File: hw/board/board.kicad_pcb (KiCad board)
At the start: 4 copper layers, 100 x 85 mm, 52 parts, among them U1 XC7A35T-FTG256, U2 TPS54331DR

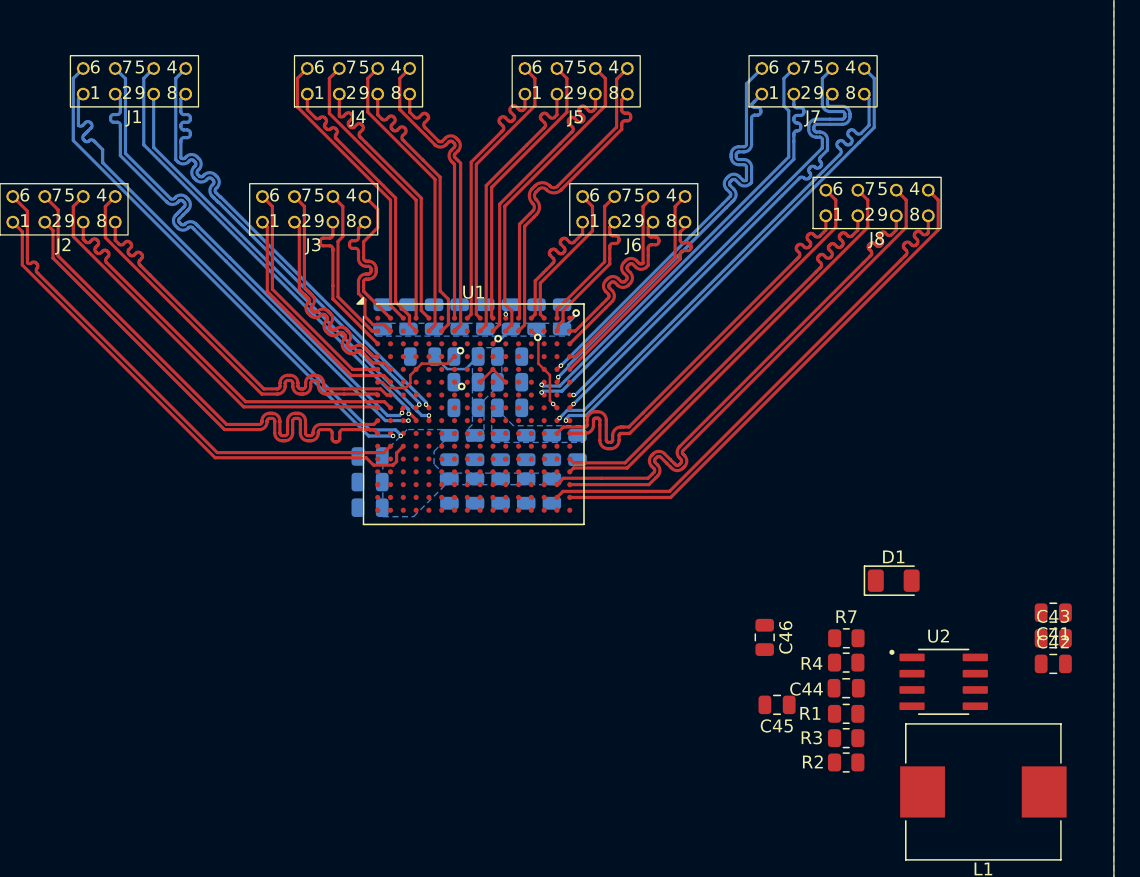
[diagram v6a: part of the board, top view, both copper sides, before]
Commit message: Routed all voltage regulators
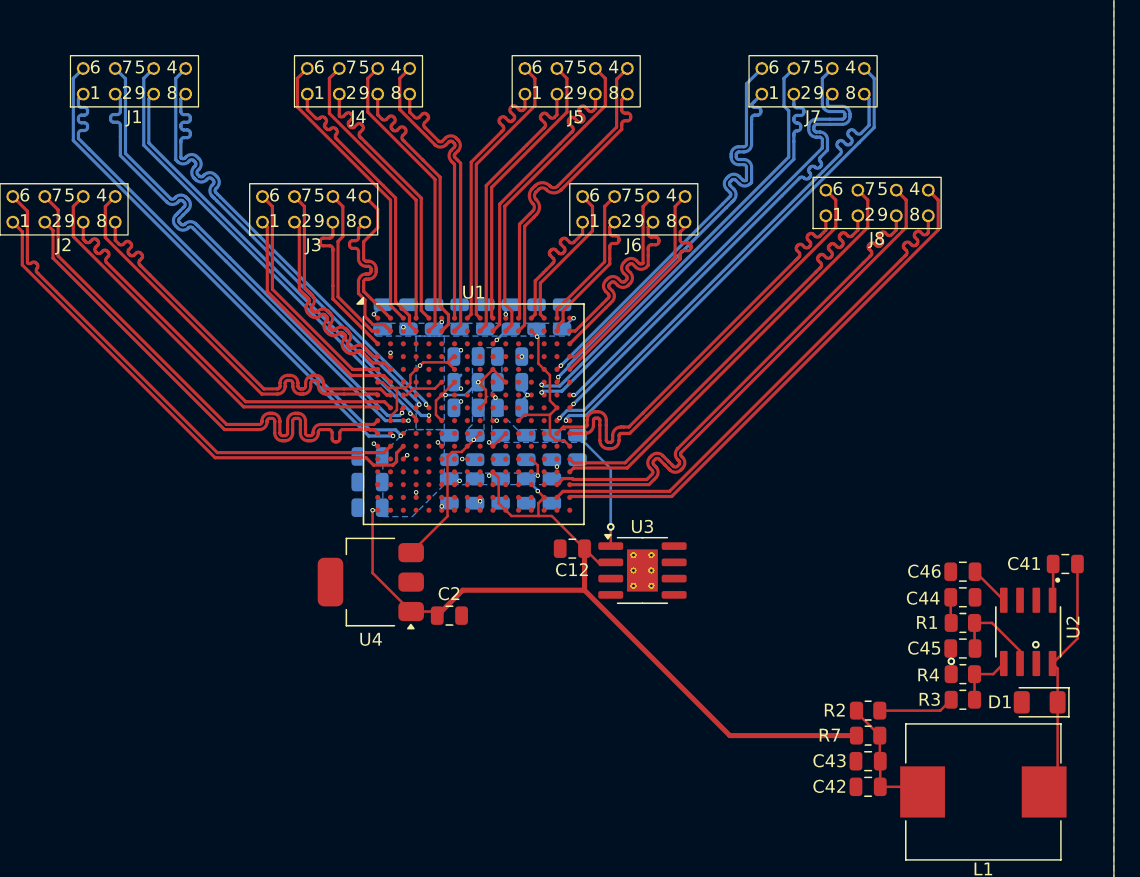
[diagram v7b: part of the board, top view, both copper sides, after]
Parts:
- added C2: 47u, Capacitor_SMD:C_0805_2012Metric, F.Cu at (132.1, 88.7)
- added U3: AP7361C-18SP-13, Package_SO:SOIC-8-1EP_3.9x4.9mm_P1.27mm_EP2.41x3.3mm_ThermalVias, F.Cu at (147.2, 85.2)
- added U4: AP7361C-10E, Package_TO_SOT_SMD:SOT-223-3_TabPin2, F.Cu at (126.0, 86.1)
- C12: value 4u7 -> 47u; moved to F.Cu
- moved C12 19.0 mm to (141.7, 83.5)
- moved C42 17.4 mm to (164.8, 102.1), turned to 180 degrees
- moved C43 17.4 mm to (164.8, 100.1), turned to 180 degrees
- moved C46 16.3 mm to (172.2, 85.3), turned to 180 degrees
- moved C45 15.2 mm to (172.2, 91.3)
- moved D1 14.8 mm to (178.2, 95.5), turned to 180 degrees
- moved R1 11.6 mm to (172.2, 89.3)
- moved C44 11.6 mm to (172.2, 87.3)
- moved R3 9.59 mm to (172.2, 95.3), turned to 0 degrees
- moved R4 9.16 mm to (172.2, 93.3)
- moved R7 7.79 mm to (164.8, 98.1), turned to 180 degrees
- moved U2 7.67 mm to (177.3, 90.0), turned to -90 degrees
- moved R2 4.40 mm to (164.8, 96.2)
- moved C41 3.91 mm to (180.2, 84.7)
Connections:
- C12 pad 1: +1V0 -> VCCO_14
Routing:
- net VCCO_14: track 19.3 -> 105.1 mm, vias 4 -> 14
- net Net-(D1-K): track 0.00 -> 19.2 mm
- net +1V0: track 7.04 -> 24.4 mm, vias 0 -> 3
- net +1V8: track 0.00 -> 13.3 mm, vias 0 -> 4
- net Net-(C42-Pad1): track 0.00 -> 10.2 mm
- net GND: track 2.75 -> 11.8 mm, vias 3 -> 15
- net Net-(U2-COMP): track 0.00 -> 7.46 mm
- net Net-(R2-Pad2): track 0.00 -> 5.93 mm
- net Net-(U2-VSENSE): track 0.00 -> 4.63 mm
- net Net-(U2-SS): track 0.00 -> 3.17 mm
- net Net-(U2-BOOT): track 0.00 -> 2.85 mm
- net Net-(C44-Pad1): track 0.00 -> 2.02 mm

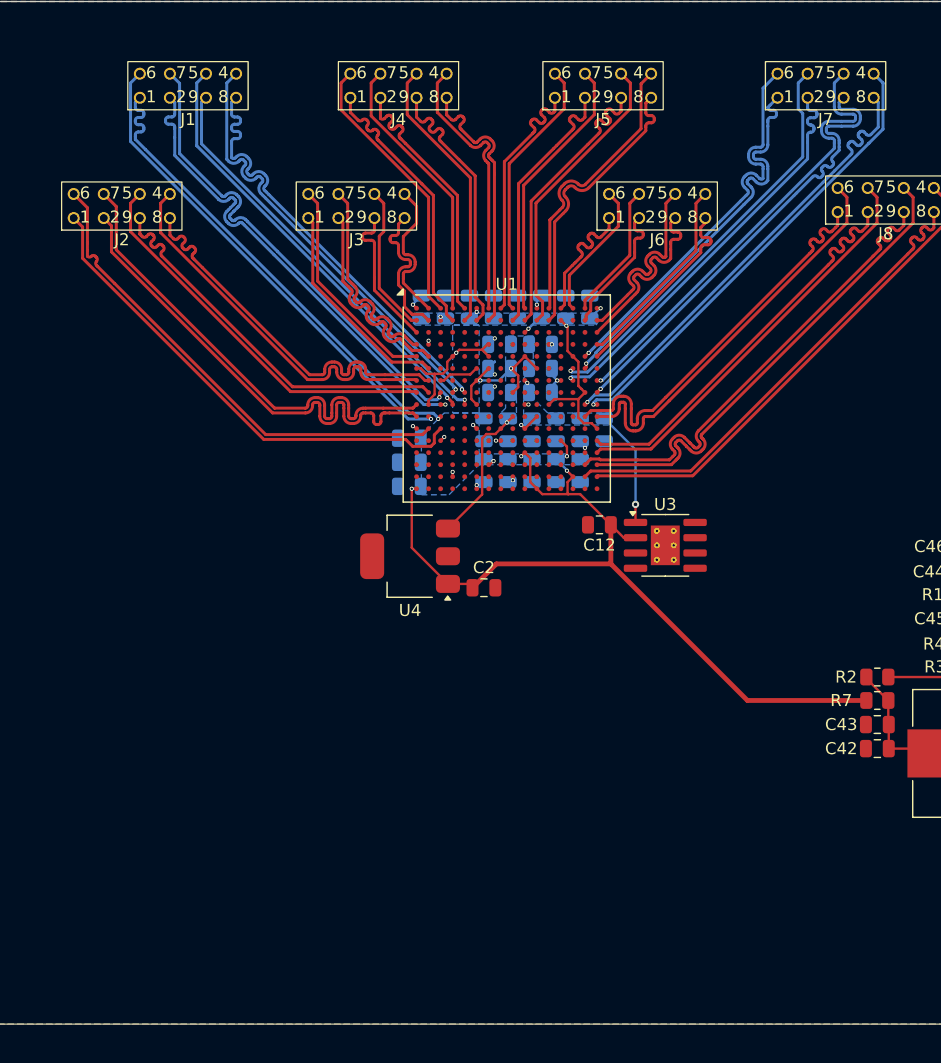
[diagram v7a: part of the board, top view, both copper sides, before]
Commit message: Finished routing STM32 connection, resolved DRC errors
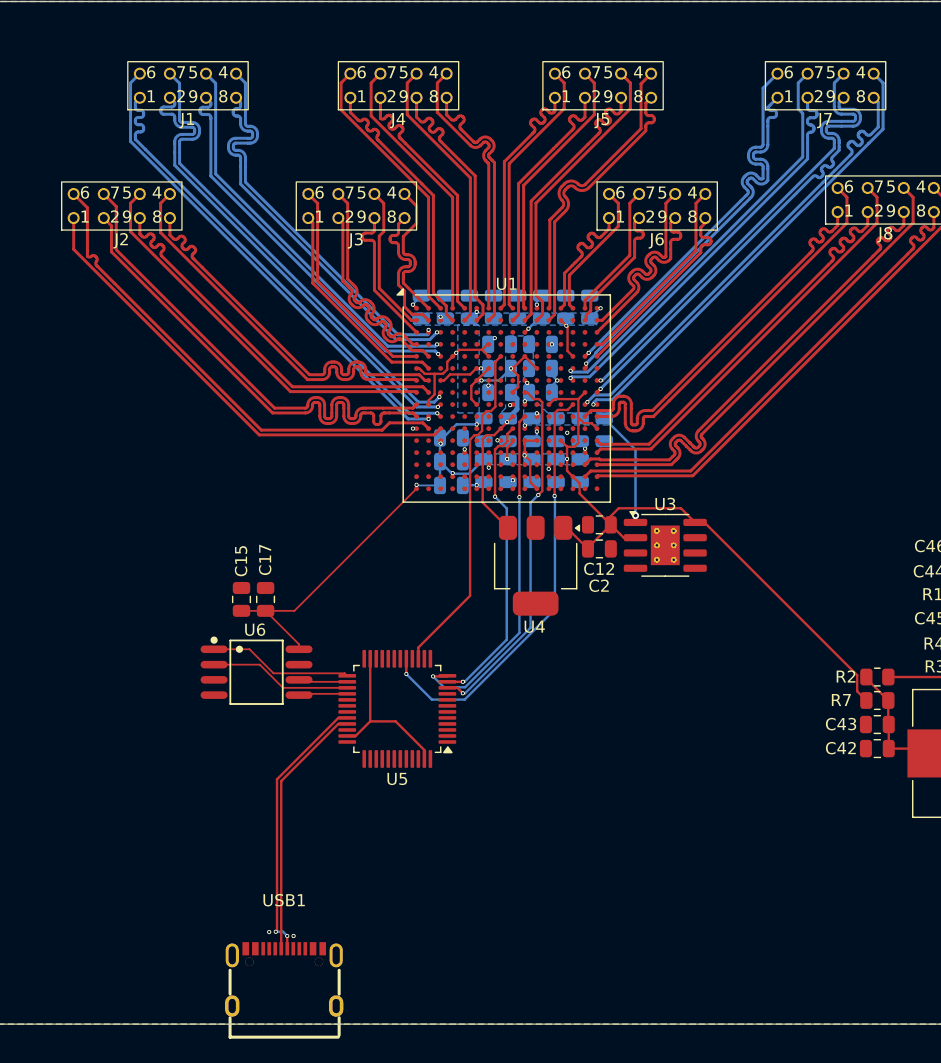
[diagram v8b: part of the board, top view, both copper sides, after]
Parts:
- added C15: 47u, Capacitor_SMD:C_0805_2012Metric, F.Cu at (112.0, 89.7)
- added C17: 470n, Capacitor_SMD:C_0805_2012Metric, F.Cu at (114.0, 89.7)
- added U5: STM32F302CBTx, Package_QFP:LQFP-48_7x7mm_P0.5mm, F.Cu at (124.9, 98.8)
- added U6: W25Q128JVSIQTR, EasyEDA:SOIC-8_L5.3-W5.3-P1.27-LS8.0-BL, F.Cu at (113.2, 95.8)
- added USB1: TYPE-C 16PIN 2MD(073), EasyEDA:USB-C-SMD_TYPE-C-6PIN-2MD-073, F.Cu at (115.5, 121.1)
- moved U4 10.5 mm to (136.4, 86.9), turned to -90 degrees
- moved C2 10.1 mm to (141.7, 85.5)
- moved C36 3.50 mm to (129.4, 80.2), turned to 0 degrees
- moved C37 3.50 mm to (129.4, 78.2), turned to 0 degrees
- moved C35 3.50 mm to (129.4, 76.3), turned to 0 degrees
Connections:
- U1 pad C2: unconnected-(U1B-IO_L7N_T1_AD6N_35-PadC2) -> S_{out}1_N
- U1 pad C3: unconnected-(U1B-IO_L7P_T1_AD6P_35-PadC3) -> S_{out}1_P
- U1 pad D3: unconnected-(U1B-IO_L11N_T1_SRCC_35-PadD3) -> D_{out}1_N
- U1 pad E3: unconnected-(U1B-IO_L11P_T1_SRCC_35-PadE3) -> D_{out}1_P
- U1 pad E8: unconnected-(U1C-CCLK_0-PadE8) -> CCLK
- U1 pad H10: unconnected-(U1C-DONE_0-PadH10) -> DONE
- U1 pad H4: S_{out}1_N -> unconnected-(U1B-IO_L18N_T2_35-PadH4)
- U1 pad H5: S_{out}1_P -> unconnected-(U1B-IO_L18P_T2_35-PadH5)
- U1 pad J14: unconnected-(U1A-IO_L1N_T0_D01_DIN_14-PadJ14) -> DIN
- U1 pad J4: D_{out}1_N -> unconnected-(U1B-IO_L19N_T3_VREF_35-PadJ4)
- U1 pad J5: D_{out}1_P -> unconnected-(U1B-IO_L19P_T3_35-PadJ5)
- U1 pad K10: unconnected-(U1C-INIT_B_0-PadK10) -> INIT_B
- U1 pad L7: unconnected-(U1C-TCK_0-PadL7) -> TCK
- U1 pad L9: unconnected-(U1C-PROGRAM_B_0-PadL9) -> PROGRAM_B
- U1 pad M10: unconnected-(U1C-M1_0-PadM10) -> VCCO_14
- U1 pad M11: unconnected-(U1C-M2_0-PadM11) -> VCCO_14
- U1 pad M7: unconnected-(U1C-TMS_0-PadM7) -> TMS
- U1 pad M9: unconnected-(U1C-M0_0-PadM9) -> VCCO_14
- U1 pad N7: unconnected-(U1C-TDI_0-PadN7) -> TDI
- U1 pad N8: unconnected-(U1C-TDO_0-PadN8) -> TDO
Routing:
- net DIN: track 0.00 -> 35.7 mm, vias 0 -> 2
- net DONE: track 0.00 -> 30.3 mm, vias 0 -> 2
- net INIT_B: track 0.00 -> 28.8 mm, vias 0 -> 2
- net CCLK: track 0.00 -> 28.4 mm
- net PROGRAM_B: track 0.00 -> 25.2 mm, vias 0 -> 2
- net USB_D_N: track 0.00 -> 22.8 mm, vias 0 -> 2
- net USB_D_P: track 0.00 -> 21.4 mm
- net VCCO_14: track 105.1 -> 122.8 mm
- net Net-(U5-VSS-Pad23): track 0.00 -> 13.8 mm
- net ~{FLASH_CS}: track 0.00 -> 12.0 mm
- net FLASH_MISO: track 0.00 -> 11.9 mm
- net GND: track 11.8 -> 16.7 mm, vias 15 -> 21
- net FLASH_SCK: track 0.00 -> 4.08 mm
- net FLASH_MOSI: track 0.00 -> 4.05 mm
- net S_{out}1_N: track 37.1 -> 33.3 mm
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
